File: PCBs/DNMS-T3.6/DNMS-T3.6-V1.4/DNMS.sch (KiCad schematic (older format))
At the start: 14 parts, among them J1 Conn_01x02, J2 Conn_02x03_Odd_Even, J3 Conn_01x04, J4 Conn_01x01, J5 RJ12, J6 RJ12, U1 Teensy3.6, U2 P82B715PN,112, U3 P82B715DR

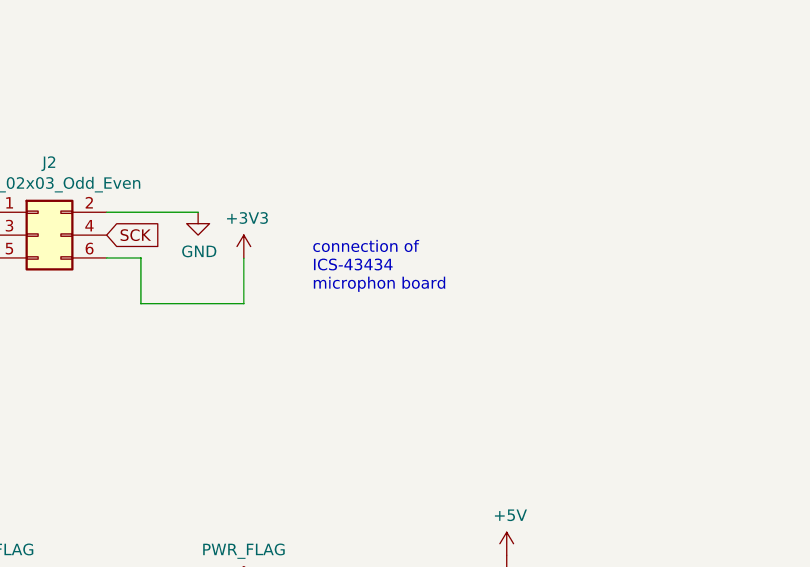
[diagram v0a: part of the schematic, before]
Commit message: spelling changes
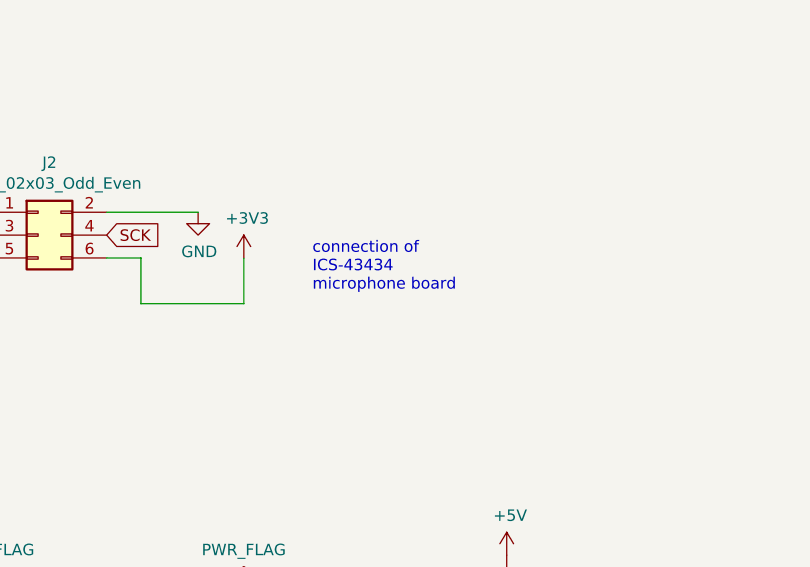
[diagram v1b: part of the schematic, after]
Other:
- note added: "connection of\nICS-43434\nmicrophone board\n"
- note removed: "connection of\nICS-43434\nmicrophon board\n"
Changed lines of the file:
@@
 I²C\nconnection
 Text Notes 4650 5250 0    50   ~ 0
-connection of\nICS-43434\nmicrophon board\n
+connection of\nICS-43434\nmicrophone board\n
 Wire Wire Line
 	7100 1850 7350 1850
